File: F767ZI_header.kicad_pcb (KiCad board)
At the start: 2 copper layers, 24 parts, among them J1 I2C2_MD, J2 CAN1, J3 CAN2, J4 UART, J5 PowerBoard, J6 EMERSW_CON, J7 I2C1_default, J9 RESET_SW, SW1 SW_Push, U1 MCP2562-E-P, U2 MCP2562-E-P

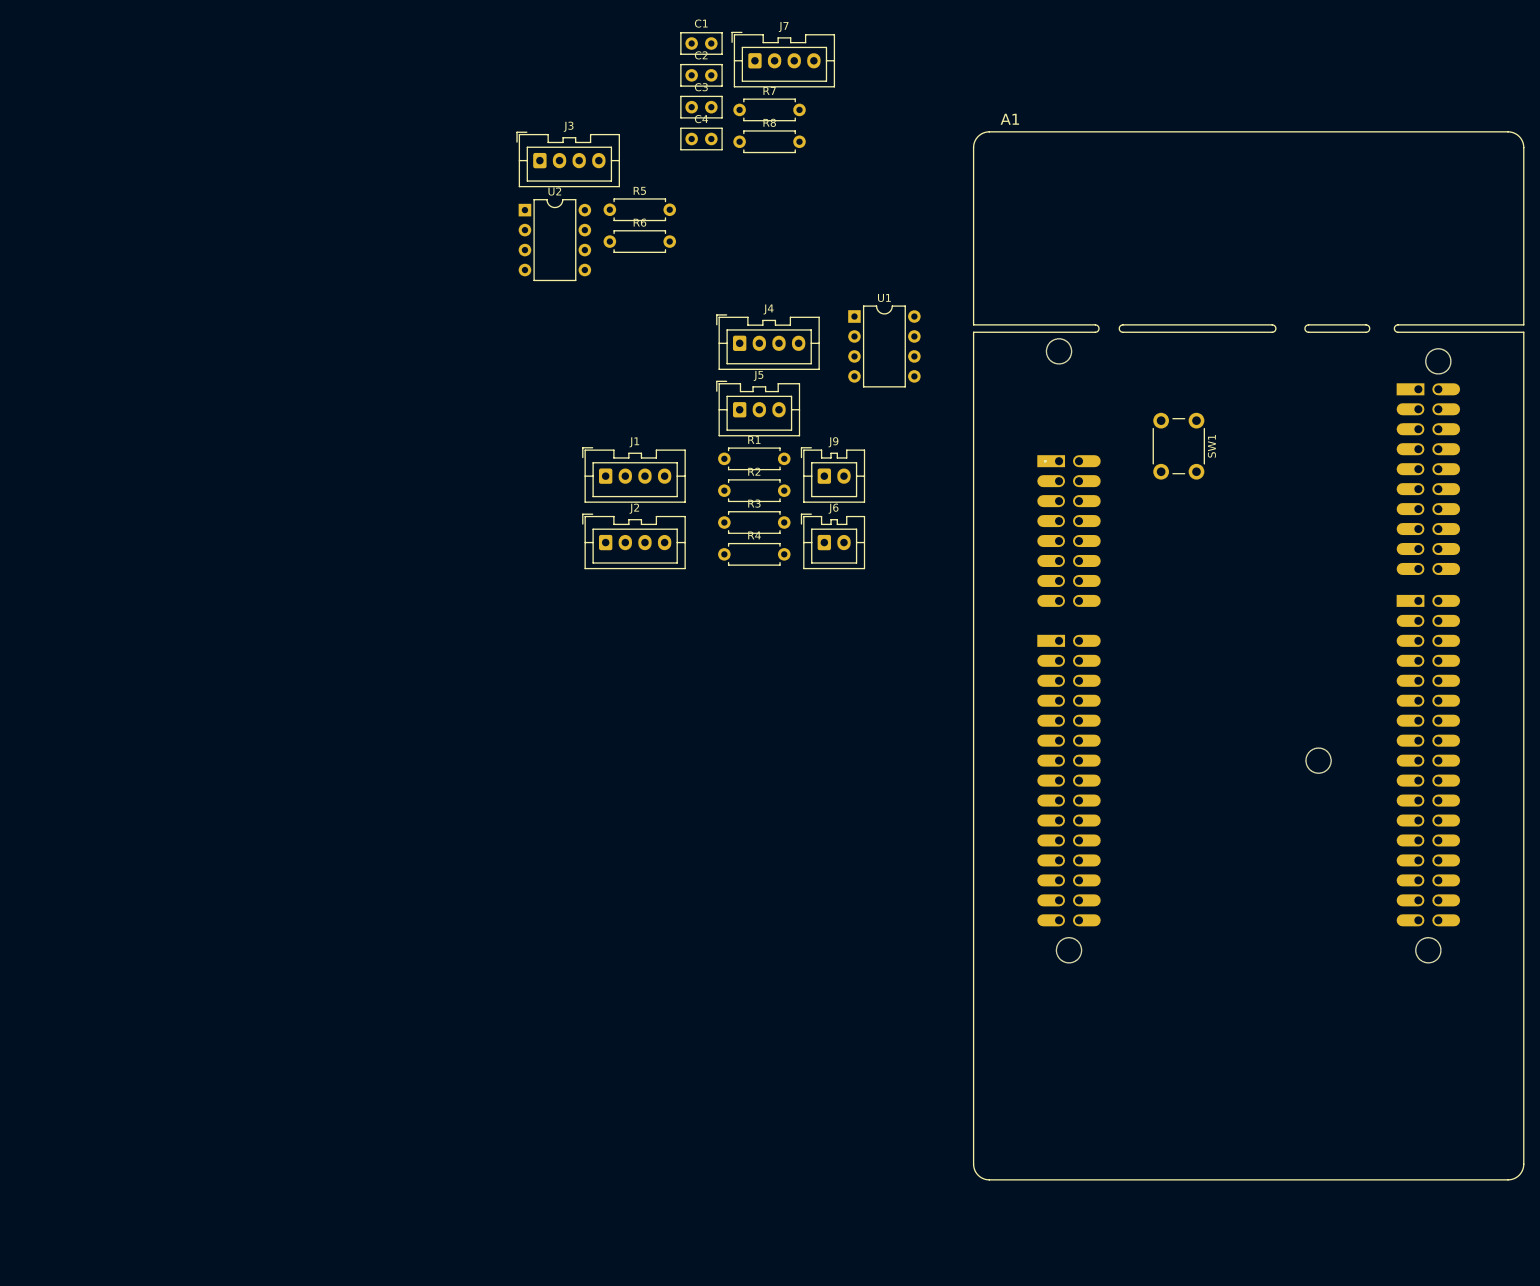
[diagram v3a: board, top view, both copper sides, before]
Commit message: PCB: Wired up all
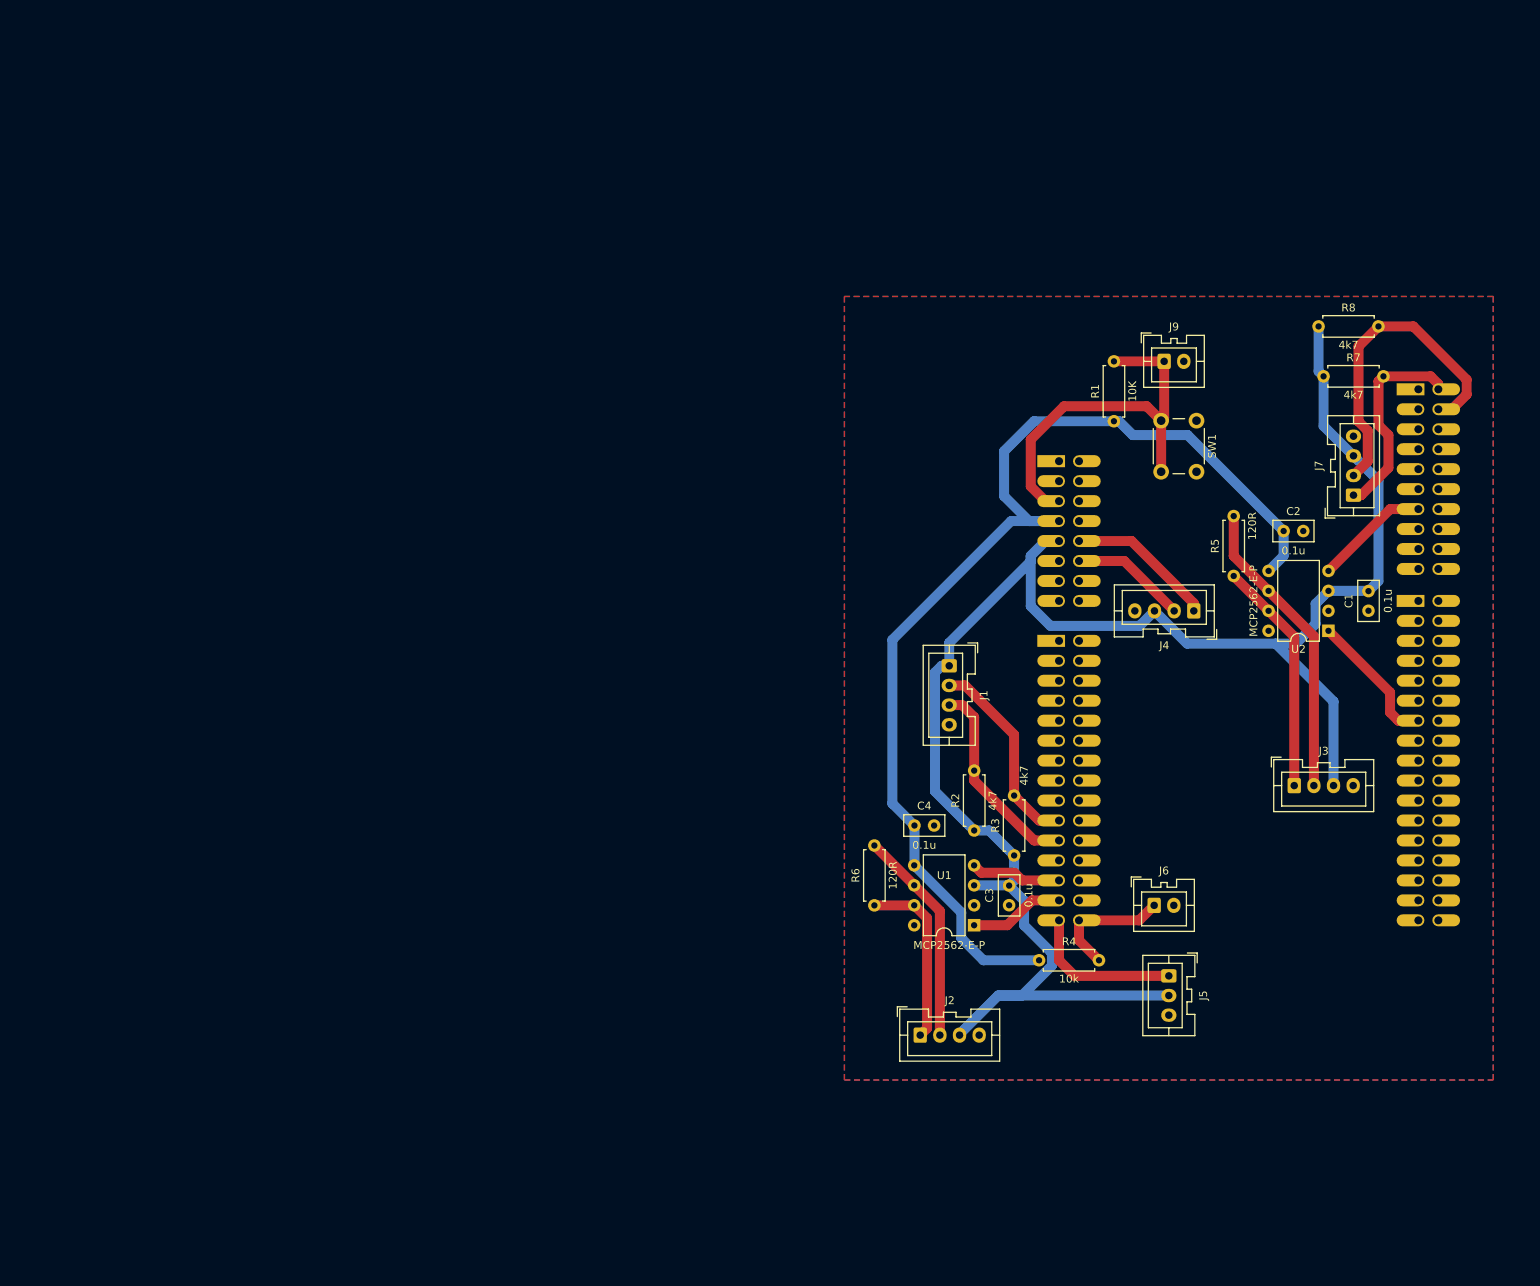
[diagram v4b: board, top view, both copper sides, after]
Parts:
- moved J3 124.6 mm to (202.0, 111.8)
- moved U2 115.4 mm to (206.4, 92.1), turned to 180 degrees
- moved C1 110.8 mm to (211.5, 87.0), turned to -90 degrees
- moved C3 107.0 mm to (165.7, 124.5), turned to -90 degrees
- moved C2 95.0 mm to (200.7, 79.4)
- moved J7 94.1 mm to (209.6, 74.8), turned to 90 degrees
- moved R5 92.0 mm to (194.3, 85.1), turned to 90 degrees
- moved C4 91.8 mm to (153.7, 116.8)
- moved R6 90.9 mm to (148.6, 127.0), turned to 90 degrees
- moved J5 90.4 mm to (186.1, 136.0), turned to -90 degrees
- moved R7 81.7 mm to (205.7, 59.7)
- moved U1 78.9 mm to (161.3, 129.5), turned to 180 degrees
- moved R8 77.3 mm to (205.1, 53.3)
- moved J2 74.4 mm to (154.4, 143.5)
- moved J4 67.1 mm to (189.2, 89.5), turned to 180 degrees
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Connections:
- J2 pad 4: Net-(J2-Pin_4) -> GND
- J3 pad 4: Net-(J2-Pin_4) -> GND
- J4 pad 4: Net-(J2-Pin_4) -> GND
- J7 pad 4: Net-(J2-Pin_4) -> GND
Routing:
- net +5V: track 0.00 -> 229.1 mm
- net +3V3: track 0.00 -> 143.0 mm
- net NRST: track 0.00 -> 50.0 mm
- net I2C1_SDA: track 0.00 -> 41.6 mm
- net CAN2L: track 0.00 -> 38.5 mm
- net CAN2H: track 0.00 -> 29.9 mm
- net CAN1L: track 0.00 -> 27.6 mm
- net I2C1_SCL: track 0.00 -> 26.4 mm
- net I2C2_SDA: track 0.00 -> 25.8 mm
- net I2C2_SCL: track 0.00 -> 25.6 mm
- net CAN1H: track 0.00 -> 22.6 mm
- net EMER_SIG: track 0.00 -> 19.9 mm
- net UART_TX: track 0.00 -> 18.9 mm
- net CAN2_TD: track 0.00 -> 17.7 mm
- net EMER_SW: track 0.00 -> 16.5 mm
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- added copper zone on B.Cu, net GND
- added copper zone on F.Cu, net GND

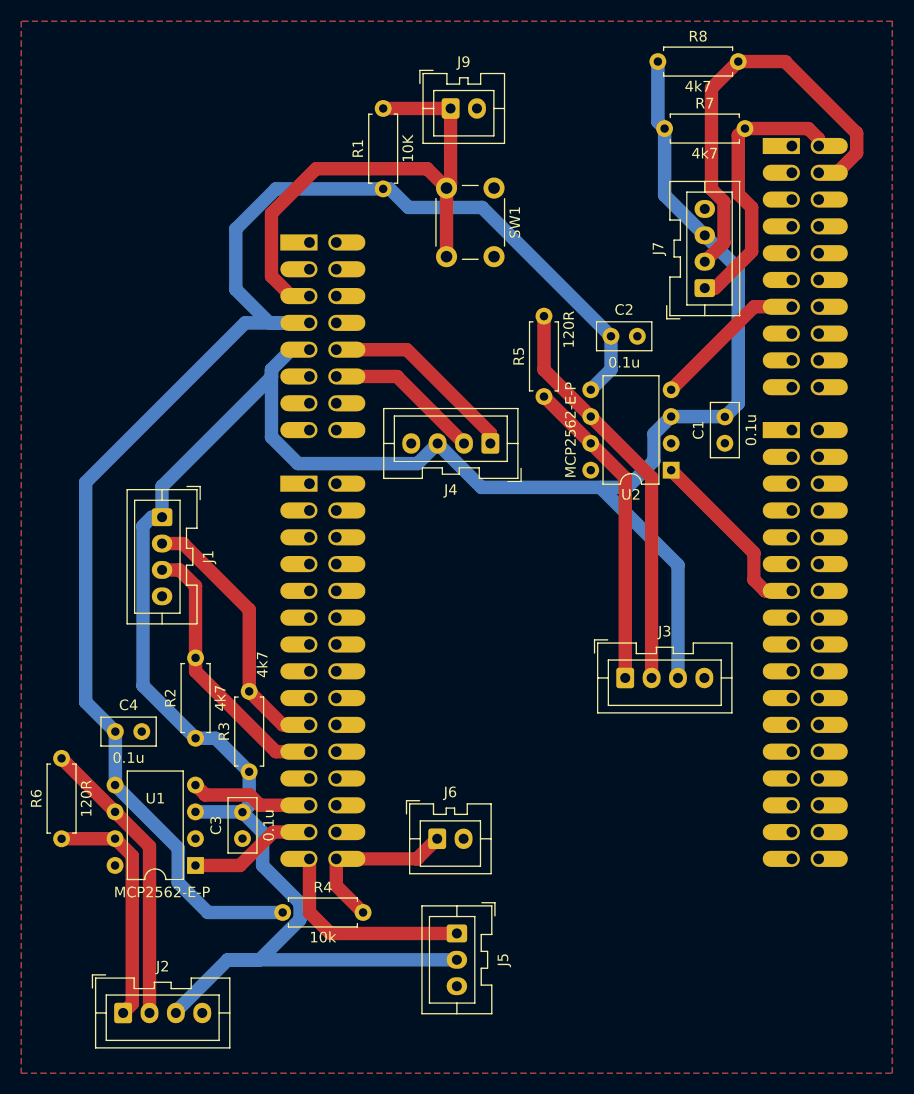
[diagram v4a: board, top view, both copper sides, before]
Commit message: PCB: Place Connectors around the perimeter
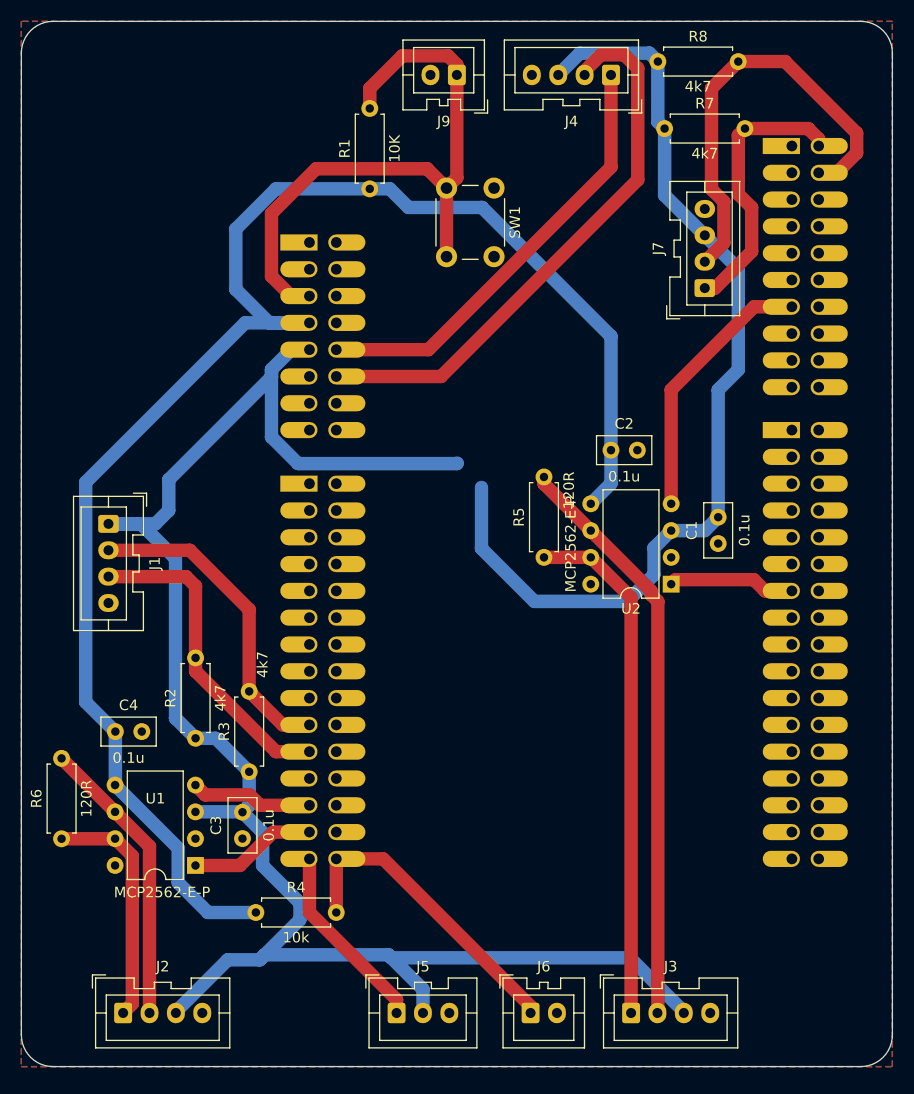
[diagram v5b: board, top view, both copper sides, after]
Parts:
- moved J4 36.7 mm to (200.7, 54.6)
- moved J3 31.8 mm to (202.6, 143.5)
- moved J6 18.7 mm to (193.0, 143.5)
- moved R5 15.2 mm to (194.3, 100.3)
- moved U2 10.8 mm to (206.4, 102.9)
- moved C2 10.8 mm to (200.7, 90.2)
- moved C1 9.53 mm to (210.8, 96.5)
- moved J5 9.46 mm to (180.3, 143.5), turned to 0 degrees
- moved J1 5.12 mm to (153.0, 97.2)
- moved J9 3.23 mm to (186.1, 54.6), turned to 180 degrees
- moved R4 2.54 mm to (167.0, 134.0)
- moved R1 1.27 mm to (177.8, 57.8)
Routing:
- net UART_RX: track 14.7 -> 53.4 mm
- net +5V: track 229.1 -> 265.8 mm
- net UART_TX: track 18.9 -> 41.9 mm
- net CAN2H: track 29.9 -> 49.2 mm
- net CAN2L: track 38.5 -> 55.3 mm
- net EMER_SW: track 16.5 -> 29.9 mm
- net CAN2_RD: track 14.7 -> 25.5 mm
- net NRST: track 50.0 -> 59.8 mm
- net +3V3: track 143.0 -> 151.3 mm
- net CAN2_TD: track 17.7 -> 12.1 mm
- net I2C2_SDA: track 25.8 -> 30.6 mm
- net I2C2_SCL: track 25.6 -> 30.4 mm
- net EMER_SIG: track 19.9 -> 18.0 mm
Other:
- board outline added: 82.6 x 99.1 mm

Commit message: PCB: 詳細なシルクを追加
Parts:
- moved R5 2.84 mm to (191.8, 99.1)
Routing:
- net +5V: track 265.8 -> 269.0 mm
- net CAN2H: track 49.2 -> 52.3 mm
- net CAN2L: track 55.3 -> 58.0 mm
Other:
- board text added: "+5V SCL SDA GND"
- board text added: "CANH CANL +5V GND"
- board text added: "EMER_SW"
- board text added: "GND +5V SDA SCL"
- board text added: "MD"
- board text added: "PowerBoard"

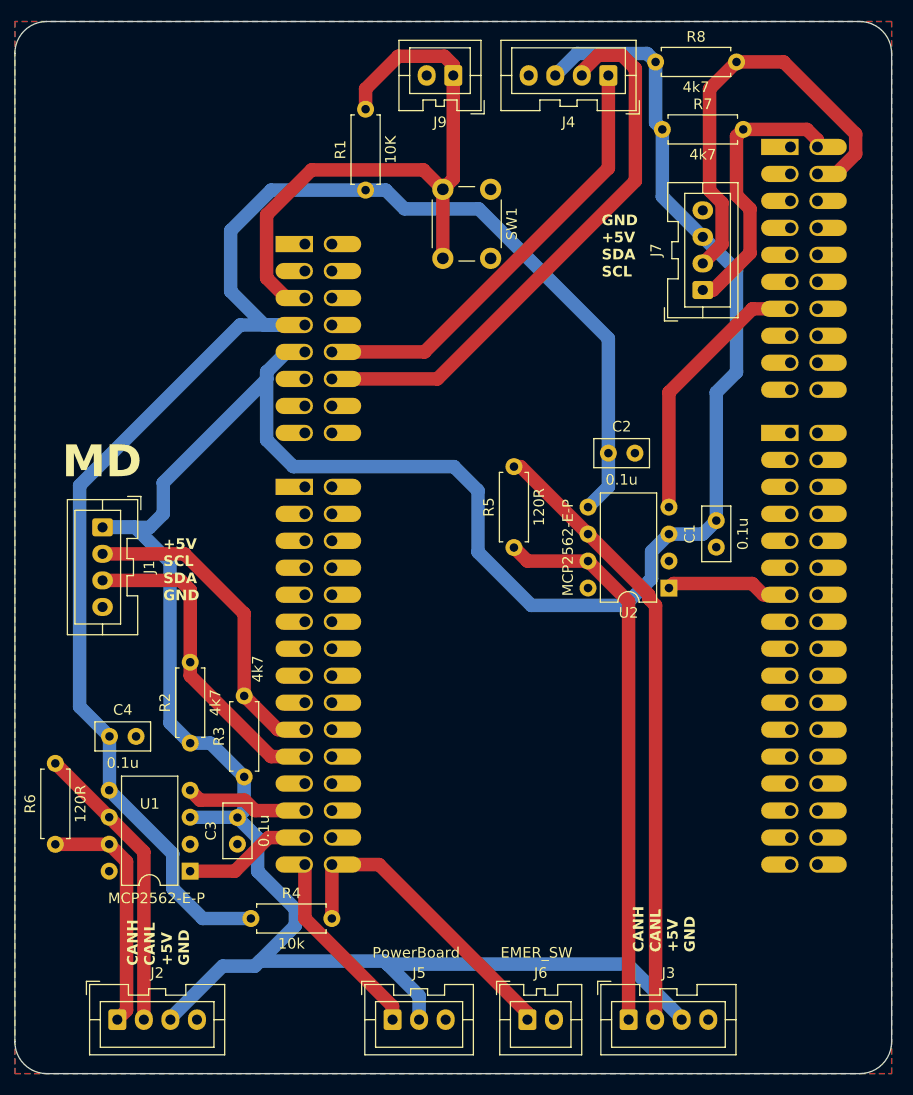
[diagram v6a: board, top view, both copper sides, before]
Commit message: PCB: 発注用のシルクとロゴを追加
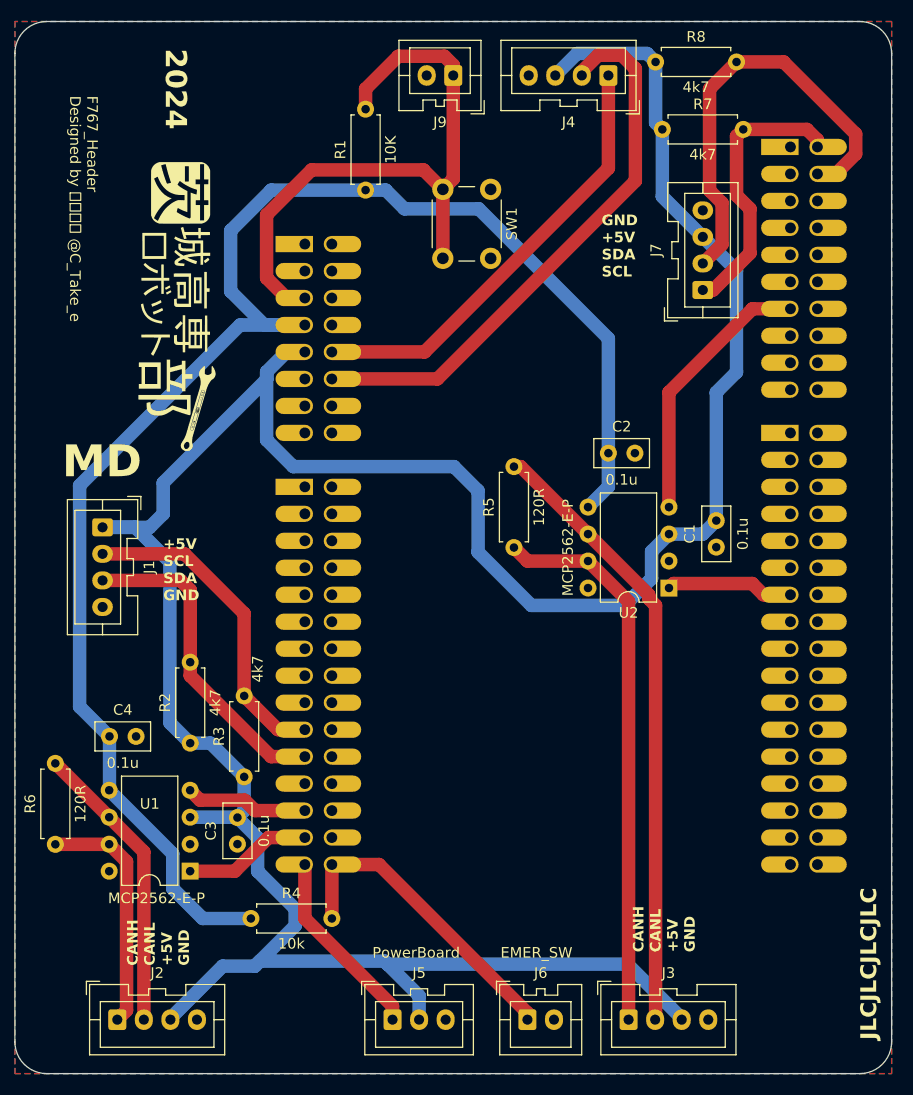
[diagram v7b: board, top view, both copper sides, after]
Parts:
- added G***: LOGO, LOGO, F.Cu at (160.0, 76.8)
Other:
- board text added: "2024"
- board text added: "F767_Header Designed by しーたけ @C_Take_e"
- board text added: "JLCJLCJLCJLC"
